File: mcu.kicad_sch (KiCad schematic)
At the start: 22 parts, among them U2 ST STM32H563VIT6, Y1 Crystal

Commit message: edit symbols because of DRC errors (DRV and LM5164)
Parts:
- D6: value LED_Status -> LED_Error
- R30, R31: value 220 -> 330; LCSC Part # C22962 -> C23138

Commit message: update pcb (no errors with XRC)
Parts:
- added C34: 100n, Capacitor_SMD:C_0603_1608Metric, symbol Device:C
- added J3: Conn_ARM_JTAG_SWD_10, Connector_PinHeader_1.27mm:PinHeader_2x05_P1.27mm_Vertical, symbol Connector:Conn_ARM_JTAG_SWD_10
- added R33, R35: 10k, Resistor_SMD:R_0805_2012Metric_Pad1.20x1.40mm_HandSolder, symbol Device:R
- C13, C15: footprint Capacitor_SMD:C_0201_0603Metric -> Capacitor_SMD:C_0603_1608Metric
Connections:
- net +3.3V: now also J3.1 (VTref), R35.1
- net GND: now also C34.2, J3.3 (GND), J3.5 (GND), J3.9 (GNDDetect), R33.1
- net SPI_MISO: now also U2.79 (PC11); no longer U2.90 (PB4(NJTRST))
- net SPI_MOSI: now also U2.80 (PC12); no longer U2.91 (PB5)
- net SPI_SCK: now also U2.78 (PC10); no longer U2.89 (PB3(JTDO)
- net SWCLK: now also J3.4 (SWCLK/TCK)
- net SWDIO: now also J3.2 (SWDIO/TMS)
- net Reset: now reaches U2.14 (NRST)
- net Reset: now also C34.1, J3.10 (~{RESET}), R35.2
- net at U2.94 (BOOT0): now also R33.2
- new net SWO: J3.6 (SWO/TDO), U2.89 (PB3(JTDO)
- no-connect marks 52 -> 50

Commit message: finished design of PCB
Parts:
- C13, C15: LCSC Part # C1663 -> https://jlcpcb.com/partdetail/2015-CL10C330JB8NNNC/C1663
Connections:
- net GND: now also C13.2, C15.2; no longer C13.1, C15.1
- net RCC_OSC_IN: now also C13.1; no longer C13.2
- net RCC_OSC_OUT: now also C15.1; no longer C15.2

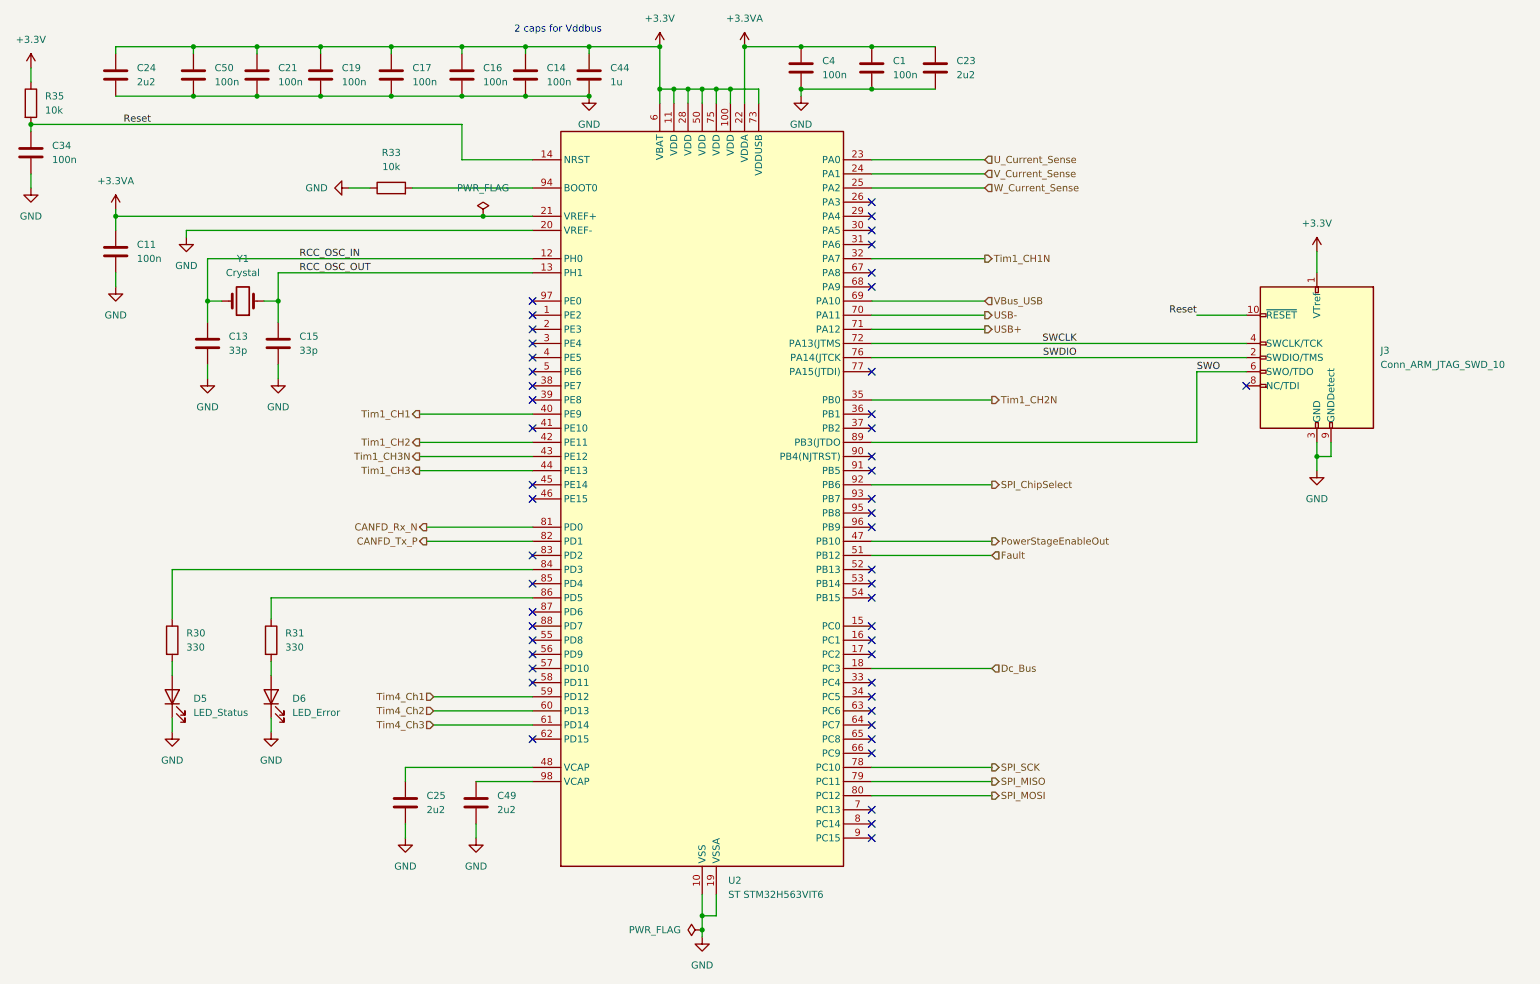
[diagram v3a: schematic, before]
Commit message: changes MCU because of stock
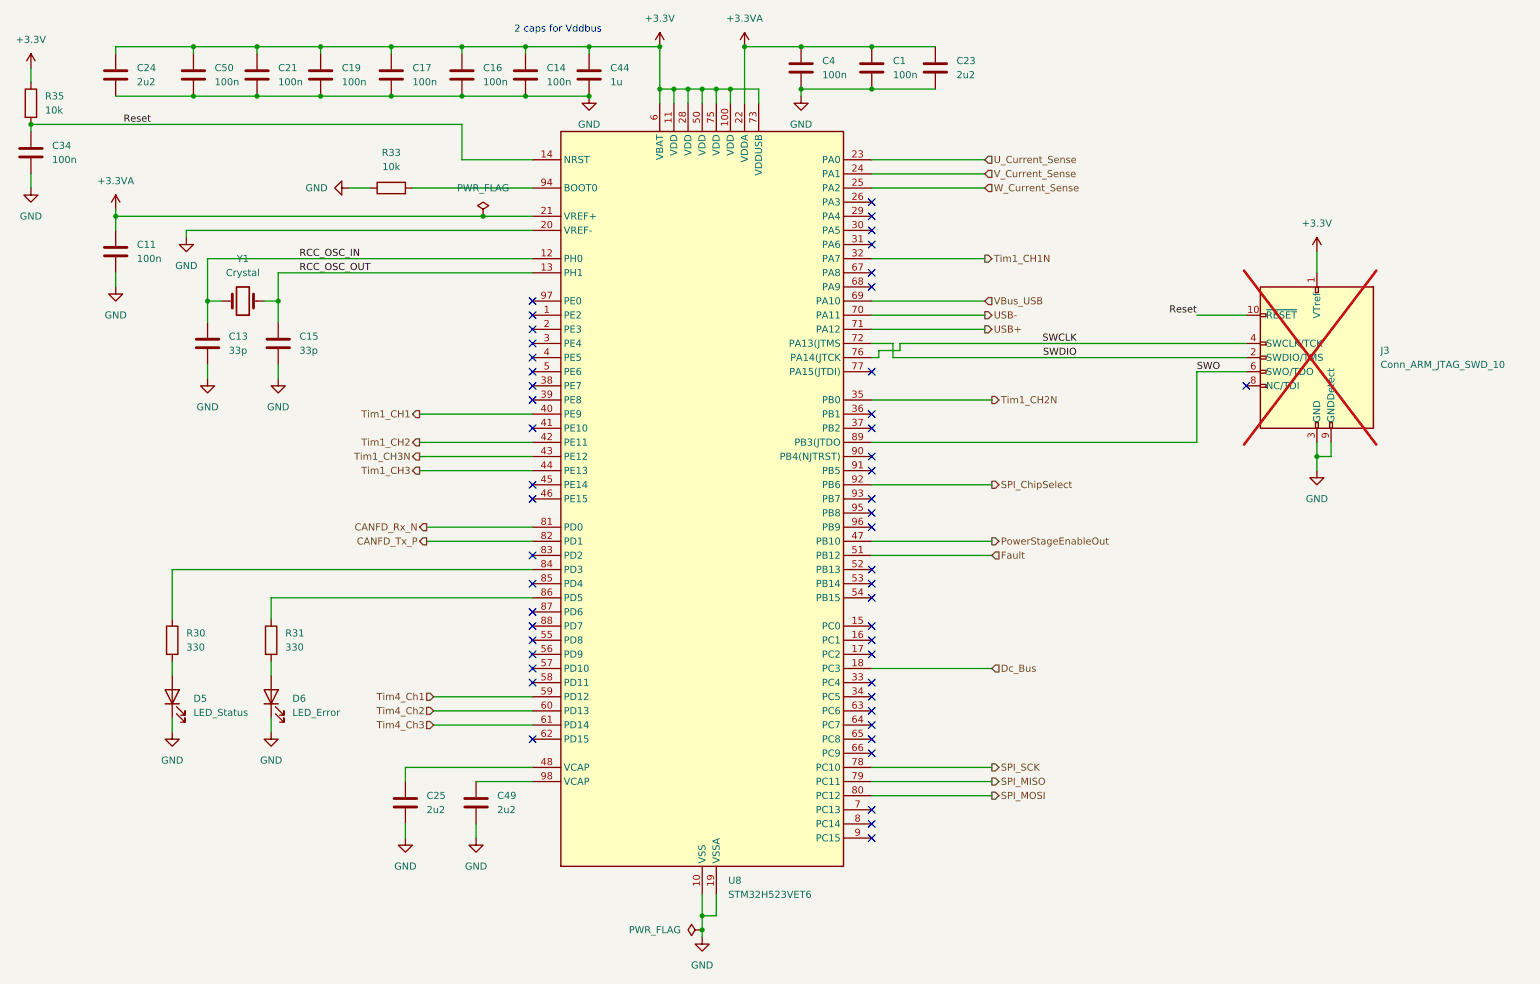
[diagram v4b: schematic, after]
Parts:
- removed U2: ST STM32H563VIT6, Package_QFP:LQFP-100_14x14mm_P0.5mm, symbol MCU_ST_STM32H5:STM32H563VITx
- added U8: STM32H523VET6, Package_QFP:LQFP-100_14x14mm_P0.5mm, symbol MCU_ST_STM32H5:STM32H523VETx
- J3: now not fitted
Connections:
- net +3.3V: now also U8.100 (VDD), U8.11 (VDD), U8.28 (VDD), U8.50 (VDD), U8.6 (VBAT), U8.73 (VDDUSB), U8.75 (VDD)
- net +3.3VA: now also U8.21 (VREF+), U8.22 (VDDA)
- net CANFD_Rx_N: now also U8.81 (PD0)
- net CANFD_Tx_P: now also U8.82 (PD1)
- net Dc_Bus: now also U8.18 (PC3)
- net Fault: now also U8.51 (PB12)
- net GND: now also U8.10 (VSS), U8.19 (VSSA), U8.20 (VREF-), U8.27 (VSS), U8.49 (VSS), U8.74 (VSS), U8.99 (VSS)
- net PowerStageEnableOut: now also U8.47 (PB10)
- net RCC_OSC_IN: now also U8.12 (PH0)
- net RCC_OSC_OUT: now also U8.13 (PH1)
- net Reset: now also U8.14 (NRST)
- net SPI_ChipSelect: now also U8.92 (PB6)
- net SPI_MISO: now also U8.79 (PC11)
- net SPI_MOSI: now also U8.80 (PC12)
- net SPI_SCK: now also U8.78 (PC10)
- net SWCLK: now also U8.76 (PA14(JTCK)
- net SWDIO: now also U8.72 (PA13(JTMS)
- net SWO: now also U8.89 (PB3(JTDO)
- net Tim1_CH1: now also U8.40 (PE9)
- net Tim1_CH1N: now also U8.32 (PA7)
- net Tim1_CH2: now also U8.42 (PE11)
- net Tim1_CH2N: now also U8.35 (PB0)
- net Tim1_CH3: now also U8.44 (PE13)
- net Tim1_CH3N: now also U8.43 (PE12)
- net Tim4_Ch1: now also U8.59 (PD12)
- net Tim4_Ch2: now also U8.60 (PD13)
- net Tim4_Ch3: now also U8.61 (PD14)
- net USB+: now also U8.71 (PA12)
- net USB-: now also U8.70 (PA11)
- net U_Current_Sense: now also U8.23 (PA0)
- net VBus_USB: now also U8.69 (PA10)
- net V_Current_Sense: now also U8.24 (PA1)
- net W_Current_Sense: now also U8.25 (PA2)
- net at R30.1: now also U8.84 (PD3)
- net at C25.1: now also U8.48 (VCAP)
- net at R33.2: now also U8.94 (BOOT0)
- net at R31.1: now also U8.86 (PD5)
- net at C49.1: now also U8.98 (VCAP)
